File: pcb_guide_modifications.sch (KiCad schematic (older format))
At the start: 156 parts, among them U2 ATMEGA32U4

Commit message: Completed Schematic
Followed the guide here https://kbwiki.ai03.me/books/pcb-design/chapter/pcb-designer-guide and added to the auto generated PCB all the proper stuff that was needed.
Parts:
- removed D_, D_A, D_ALT, D_B, D_BACKSPACE, D_BSLSH, D_C, D_CAPS_LOCK, D_COMMA, D_D, D_DOT, D_E, D_ENTER, D_EQUAL, D_F, D_FN, D_G, D_H, D_I, D_J, D_K, D_L, D_M, D_MINUS, D_N, D_O, D_P, D_Q, D_QUOTE, D_R, D_S, D_SEMIC, D_SHIFT, D_SLASH, D_T, D_TAB, D_U, D_V, D_W, D_WIN, D_X, D_Y, D_Z, D_[, D_], D_`: D, keyboard_parts:D_SOD123_axial, symbol Device:D
- removed K_: KEYSW, MX_Alps_Hybrid:MX-7U-NoLED, symbol keyboard_parts:KEYSW
- removed K_A, K_B, K_BSLSH, K_C, K_COMMA, K_D, K_DOT, K_E, K_EQUAL, K_F, K_FN, K_G, K_H, K_I, K_J, K_K, K_L, K_M, K_MINUS, K_N, K_O, K_P, K_Q, K_QUOTE, K_R, K_S, K_SEMIC, K_SLASH, K_T, K_U, K_V, K_W, K_WIN, K_X, K_Y, K_Z, K_[, K_], K_`: KEYSW, MX_Alps_Hybrid:MX-1U-NoLED, symbol keyboard_parts:KEYSW
- removed K_ALT: KEYSW, MX_Alps_Hybrid:MX-1.25U-NoLED, symbol keyboard_parts:KEYSW
- removed K_BACKSPACE, K_TAB: KEYSW, MX_Alps_Hybrid:MX-1.5U-NoLED, symbol keyboard_parts:KEYSW
- removed K_CAPS_LOCK: KEYSW, MX_Alps_Hybrid:MX-1.75U-NoLED, symbol keyboard_parts:KEYSW
- removed K_ENTER, K_SHIFT: KEYSW, MX_Alps_Hybrid:MX-2.25U-NoLED, symbol keyboard_parts:KEYSW
- added D_10, D_A1, D_ALT2, D_B1, D_BACKSPACE1, D_BSLSH1, D_C1, D_CAPS_LOCK1, D_COMMA1, D_D1, D_DOT1, D_E1, D_ENTER1, D_EQUAL1, D_F11, D_FN1, D_G1, D_H1, D_I1, D_J1, D_K1, D_L1, D_M1, D_MINUS1, D_N1, D_O1, D_P1, D_Q1, D_QUOTE1, D_R1, D_S1, D_SEMIC1, D_SHIFT2, D_SLASH1, D_T1, D_TAB1, D_U1, D_V1, D_W1, D_WIN2, D_X1, D_Y1, D_Z1, D_[1, D_]1, D_`2: D, keyboard_parts:D_SOD123_axial, symbol Device:D
- added K_10: KEYSW, MX_Alps_Hybrid:MX-7U-NoLED, symbol keyboard_parts:KEYSW
- added K_A1, K_B1, K_BSLSH1, K_C1, K_COMMA1, K_D1, K_DOT1, K_E1, K_EQUAL1, K_F11, K_FN1, K_G1, K_H1, K_I1, K_J1, K_K1, K_L1, K_M1, K_MINUS1, K_N1, K_O1, K_P1, K_Q1, K_QUOTE1, K_R1, K_S1, K_SEMIC1, K_SLASH1, K_T1, K_U1, K_V1, K_W1, K_WIN2, K_X1, K_Y1, K_Z1, K_[1, K_]1, K_`2: KEYSW, MX_Alps_Hybrid:MX-1U-NoLED, symbol keyboard_parts:KEYSW
- added K_ALT2: KEYSW, MX_Alps_Hybrid:MX-1.25U-NoLED, symbol keyboard_parts:KEYSW
- added K_BACKSPACE1, K_TAB1: KEYSW, MX_Alps_Hybrid:MX-1.5U-NoLED, symbol keyboard_parts:KEYSW
- added K_CAPS_LOCK1: KEYSW, MX_Alps_Hybrid:MX-1.75U-NoLED, symbol keyboard_parts:KEYSW
- added K_ENTER1, K_SHIFT2: KEYSW, MX_Alps_Hybrid:MX-2.25U-NoLED, symbol keyboard_parts:KEYSW
- X2: renamed from Y?; value 16MHz -> XTAL_GND; footprint (none) -> Crystal:Crystal_SMD_5032-4Pin_5.0x3.2mm
- gave numbers to parts that had none: 5
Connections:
- net GND: now also USB2.5 (GND); no longer USB2.1 (VUSB)
- net VCC: now also USB2.1 (VUSB); no longer USB2.5 (GND)
- net col10: now also K_COMMA1.1, K_I1.1, K_K1.1
- net col11: now also K_DOT1.1, K_L1.1, K_O1.1
- net col12: now also K_P1.1, K_SEMIC1.1, K_SLASH1.1
- net col13: now also K_MINUS1.1, K_QUOTE1.1, K_[1.1
- net col14: now also K_ENTER1.1, K_EQUAL1.1, K_FN1.1, K_]1.1
- net col15: now also K_BACKSPACE1.1, K_BSLSH1.1
- net col2: now also K_CAPS_LOCK1.1, K_SHIFT2.1, K_TAB1.1, K_WIN2.1, K_`2.1
- net col3: now also K_A1.1, K_ALT2.1, K_Q1.1, K_Z1.1
- net col4: now also K_10.1, K_S1.1, K_W1.1, K_X1.1
- net col5: now also K_C1.1, K_D1.1, K_E1.1
- net col6: now also K_F11.1, K_R1.1, K_V1.1
- net col7: now also K_B1.1, K_G1.1, K_T1.1
- net col8: now also K_H1.1, K_N1.1, K_Y1.1
- net col9: now also K_J1.1, K_M1.1, K_U1.1
- net row0: now also D_BSLSH1.1 (K), D_EQUAL1.1 (K), D_MINUS1.1 (K), D_`2.1 (K)
- net row1: now also D_BACKSPACE1.1 (K), D_E1.1 (K), D_I1.1 (K), D_O1.1 (K), D_P1.1 (K), D_Q1.1 (K), D_R1.1 (K), D_T1.1 (K), D_TAB1.1 (K), D_U1.1 (K), D_W1.1 (K), D_Y1.1 (K), D_[1.1 (K), D_]1.1 (K)
- net row2: now also D_A1.1 (K), D_CAPS_LOCK1.1 (K), D_D1.1 (K), D_ENTER1.1 (K), D_F11.1 (K), D_G1.1 (K), D_H1.1 (K), D_J1.1 (K), D_K1.1 (K), D_L1.1 (K), D_QUOTE1.1 (K), D_S1.1 (K), D_SEMIC1.1 (K)
- net row3: now also D_B1.1 (K), D_C1.1 (K), D_COMMA1.1 (K), D_DOT1.1 (K), D_FN1.1 (K), D_M1.1 (K), D_N1.1 (K), D_SHIFT2.1 (K), D_SLASH1.1 (K), D_V1.1 (K), D_X1.1 (K), D_Z1.1 (K)
- net row4: now also D_10.1 (K), D_ALT2.1 (K), D_WIN2.1 (K)
- new net: D_]1.2 (A), K_]1.2
- new net: D_WIN2.2 (A), K_WIN2.2
- new net: D_Z1.2 (A), K_Z1.2
- new net: D_J1.2 (A), K_J1.2
- new net: D_G1.2 (A), K_G1.2
- new net: D_X1.2 (A), K_X1.2
- new net: D_CAPS_LOCK1.2 (A), K_CAPS_LOCK1.2
- new net: D_O1.2 (A), K_O1.2
- new net: D_DOT1.2 (A), K_DOT1.2
- new net: D_T1.2 (A), K_T1.2
- new net: D_TAB1.2 (A), K_TAB1.2
- new net: D_Y1.2 (A), K_Y1.2
- new net: D_ALT2.2 (A), K_ALT2.2
- new net: D_S1.2 (A), K_S1.2
- new net: D_[1.2 (A), K_[1.2
- new net: D_R1.2 (A), K_R1.2
- new net: D_10.2 (A), K_10.2
- new net: D_`2.2 (A), K_`2.2
- new net: D_M1.2 (A), K_M1.2
- new net: D_K1.2 (A), K_K1.2
- new net: D_V1.2 (A), K_V1.2
- new net: D_F11.2 (A), K_F11.2
- new net: D_SHIFT2.2 (A), K_SHIFT2.2
- new net: D_L1.2 (A), K_L1.2
- new net: D_Q1.2 (A), K_Q1.2
- new net: D_COMMA1.2 (A), K_COMMA1.2
- new net: D_U1.2 (A), K_U1.2
- new net: D_QUOTE1.2 (A), K_QUOTE1.2
- new net: D_SLASH1.2 (A), K_SLASH1.2
- new net: D_BACKSPACE1.2 (A), K_BACKSPACE1.2
- new net: D_SEMIC1.2 (A), K_SEMIC1.2
- new net: D_ENTER1.2 (A), K_ENTER1.2
- new net: D_FN1.2 (A), K_FN1.2
- new net: D_BSLSH1.2 (A), K_BSLSH1.2
- new net: D_C1.2 (A), K_C1.2
- new net: D_I1.2 (A), K_I1.2
- new net: D_W1.2 (A), K_W1.2
- new net: D_P1.2 (A), K_P1.2
- new net: D_A1.2 (A), K_A1.2
- new net: D_D1.2 (A), K_D1.2
- new net: D_E1.2 (A), K_E1.2
- new net: D_B1.2 (A), K_B1.2
- new net: D_MINUS1.2 (A), K_MINUS1.2
- new net: D_EQUAL1.2 (A), K_EQUAL1.2
- new net: D_H1.2 (A), K_H1.2
- new net: D_N1.2 (A), K_N1.2
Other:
- moved on the sheet: F1, USB2

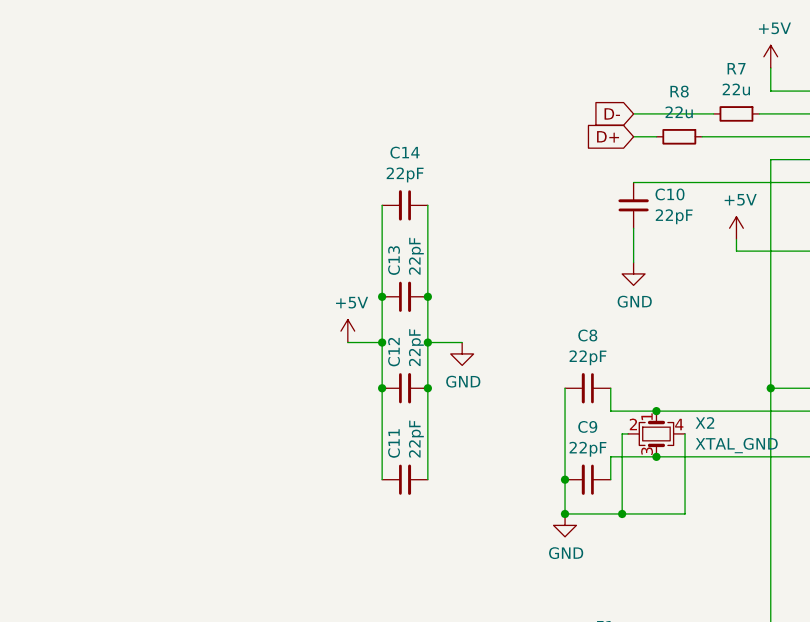
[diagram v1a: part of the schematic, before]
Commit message: Schematic with Footprints and Netlist
This is a pre check in before I attempt to import the new net list and update/add/remove components based on the schematic.
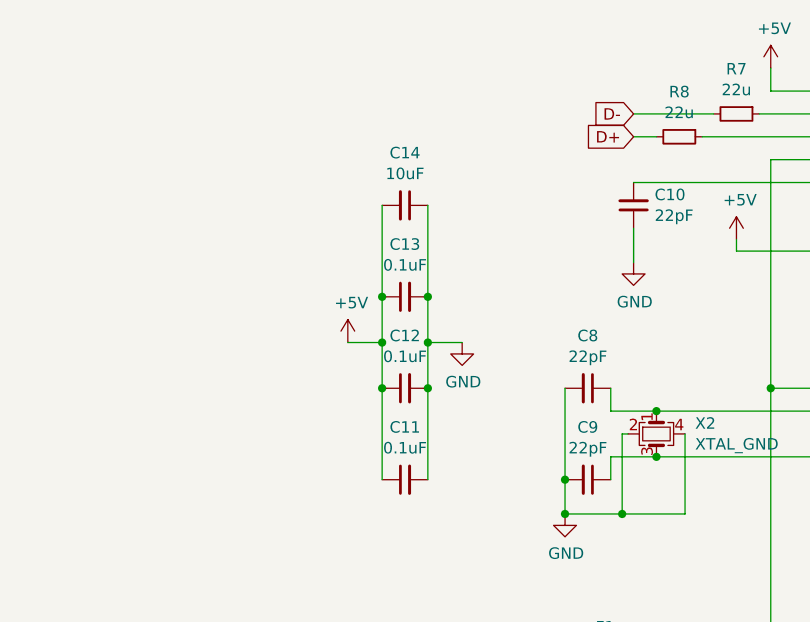
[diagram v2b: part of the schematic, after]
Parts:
- C10, C8, C9: footprint (none) -> Capacitor_SMD:C_0805_2012Metric
- C11, C12, C13: value 22pF -> 0.1uF; footprint (none) -> Capacitor_SMD:C_0805_2012Metric
- C14: value 22pF -> 10uF; footprint (none) -> Capacitor_SMD:C_0805_2012Metric
- D_0, D_1, D_10, D_2, D_3, D_4, D_5, D_6, D_7, D_8, D_9, D_A1, D_ALT1, D_ALT2, D_B1, D_BACKSPACE1, D_BSLSH1, D_C1, D_CAPS_LOCK1, D_COMMA1, D_D1, D_DOT1, D_E1, D_ENTER1, D_EQUAL1, D_F1, D_F10, D_F11, D_F2, D_F3, D_F4, D_F5, D_F6, D_F7, D_F8, D_F9, D_FN1, D_G1, D_H1, D_I1, D_J1, D_K1, D_L1, D_M1, D_MINUS1, D_N1, D_O1, D_P1, D_Q1, D_QUOTE1, D_R1, D_S1, D_SEMIC1, D_SHIFT1, D_SHIFT2, D_SLASH1, D_T1, D_TAB1, D_U1, D_V1, D_W1, D_WIN1, D_WIN2, D_X1, D_Y1, D_Z1, D_[1, D_]1, D_`1, D_`2: footprint keyboard_parts:D_SOD123_axial -> keyboard_parts:D_SOD123
- F1: footprint (none) -> Fuse_Holders_and_Fuses:Fuse_SMD1206_Reflow
- R1, R6, R7, R8: footprint (none) -> Resistor_SMD:R_0805_2012Metric
- SW1: footprint (none) -> Button_Switch_SMD:SW_SPST_TL3342
- U2: footprint (none) -> Package_QFP:TQFP-44_10x10mm_P0.8mm
- USB2: footprint (none) -> keyboard_parts:USB_miniB_hirose_5S8
